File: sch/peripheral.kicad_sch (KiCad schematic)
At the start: 7 parts, among them U1 74LVC1G139

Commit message: some docs
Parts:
- added C? (x2): 100nF, Capacitor_SMD:C_0805_2012Metric, symbol Device:C_Small
- added C?: 30pF, Capacitor_SMD:C_0805_2012Metric, symbol Device:C_Small
- added R?: 1M, Resistor_THT:R_Axial_DIN0204_L3.6mm_D1.6mm_P7.62mm_Horizontal, symbol Device:R
- added SERC?: W65C51NxQ, Package_QFP:LQFP-32_7x7mm_P0.8mm, symbol 65xx:W65C51NxQ
- added SERIAL?: Conn_02x05_Odd_Even, Connector_PinHeader_2.54mm:PinHeader_2x05_P2.54mm_Vertical, symbol Connector_Generic:Conn_02x05_Odd_Even
- added Y?: 1.8432MHz, Crystal:Crystal_HC49-4H_Vertical, symbol Device:Crystal
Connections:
- net +5V: now also C?.2, C?.2, SERC?.12 (VCC), SERC?.13 (VCC), SERIAL?.2 (Pin_2)
- net A0: now also SERC?.10 (RS0)
- net A1: now also SERC?.11 (RS1)
- net A15: now also SERC?.30 (CS1)
- net BUS_R~{W}: now also SERC?.27 (R/~{W})
- net D0: now also SERC?.16 (D0)
- net D1: now also SERC?.17 (D1)
- net D2: now also SERC?.18 (D2)
- net D3: now also SERC?.19 (D3)
- net D4: now also SERC?.20 (D4)
- net D5: now also SERC?.21 (D5)
- net D6: now also SERC?.22 (D6)
- net D7: now also SERC?.23 (D7)
- net GND: now also C?.1, C?.1, C?.2, SERC?.28 (VSS), SERC?.29 (VSS), SERIAL?.10 (Pin_10)
- net ~{RESET}: now also SERC?.32 (~{RES})
- net CLK renamed CLOCK
- net CLOCK: now also SERC?.26 (ϕ2)
- new net: R?.1, SERC?.2 (XTAL1), Y?.2
- new net: C?.1, R?.2, SERC?.3 (XTAL2), Y?.1
- new net: SERC?.1 (RxC), SERIAL?.8 (Pin_8)
- new net: SERC?.14 (~{DCD}), SERIAL?.9 (Pin_9)
- new net: SERC?.15 (~{DSR}), SERIAL?.7 (Pin_7)
- new net: SERC?.4 (~{RTS}), SERIAL?.1 (Pin_1)
- new net: SERC?.5 (~{CTS}), SERIAL?.3 (Pin_3)
- new net: SERC?.6 (TxD), SERIAL?.6 (Pin_6)
- new net: SERC?.7 (~{DTR}), SERIAL?.5 (Pin_5)
- new net: SERC?.9 (RxD), SERIAL?.4 (Pin_4)
- new net ~{SERIAL_CS}: SERC?.31 (~{CS2})
- new net ~{SRL_IRQ}: SERC?.25 (~{IRQ})
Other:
- note added: "PRP: 0x8000 - 0x8FFF SER: 0x9000 - 0x9FFF"
- note added: "Peripheral and Serial Controller"
- note added: "Serial Controller"
- moved on the sheet: C21, C22, PERIPHERAL1, PRP1, U1, USB1, USB_P1

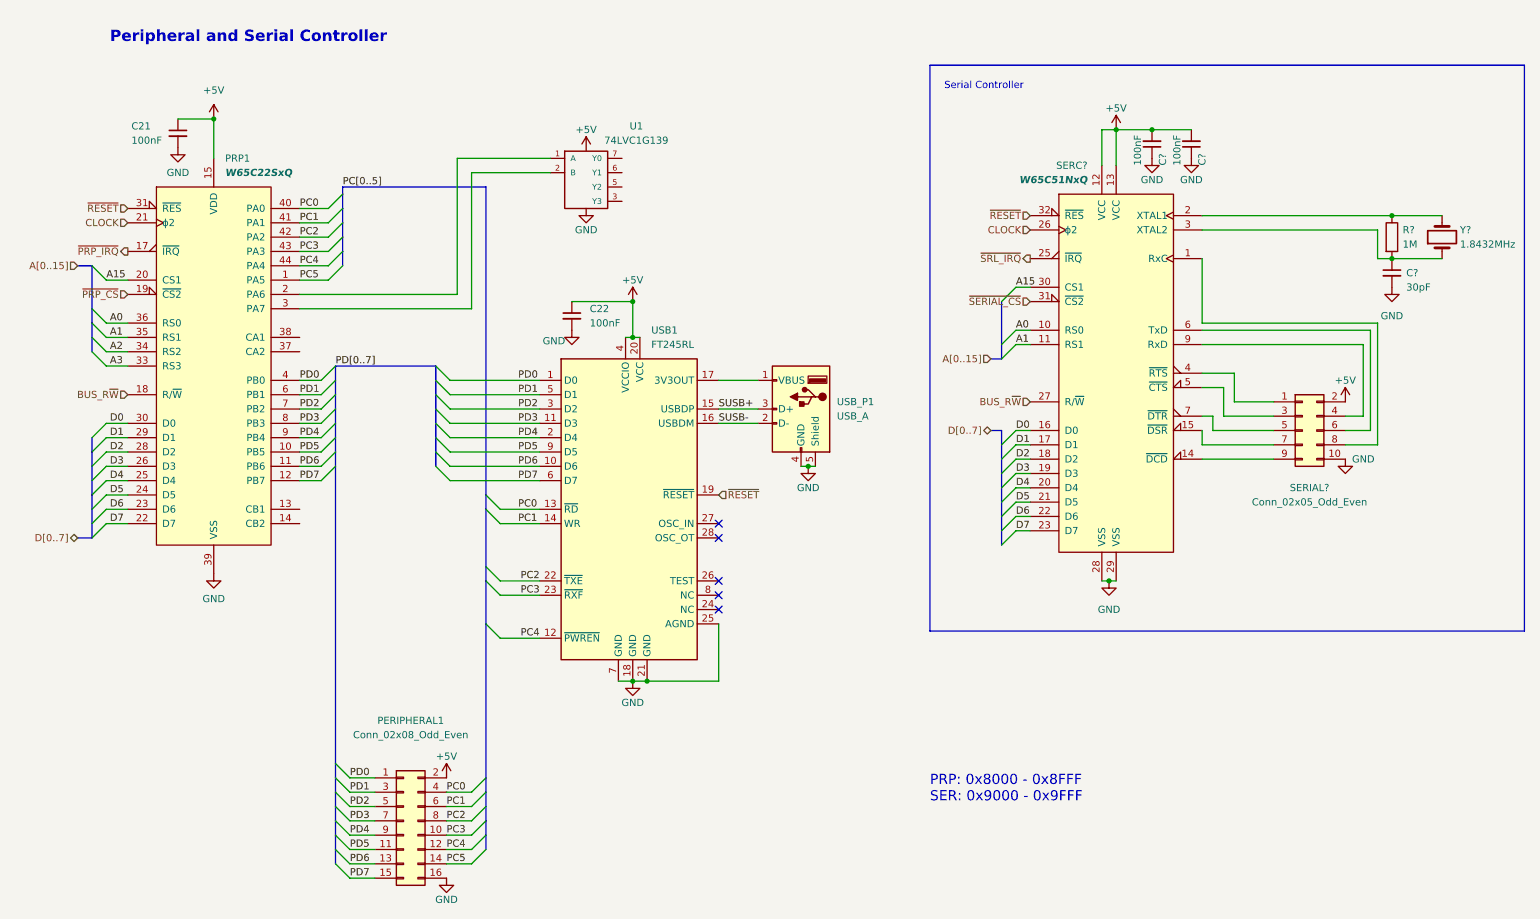
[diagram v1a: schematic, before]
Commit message: update schematic
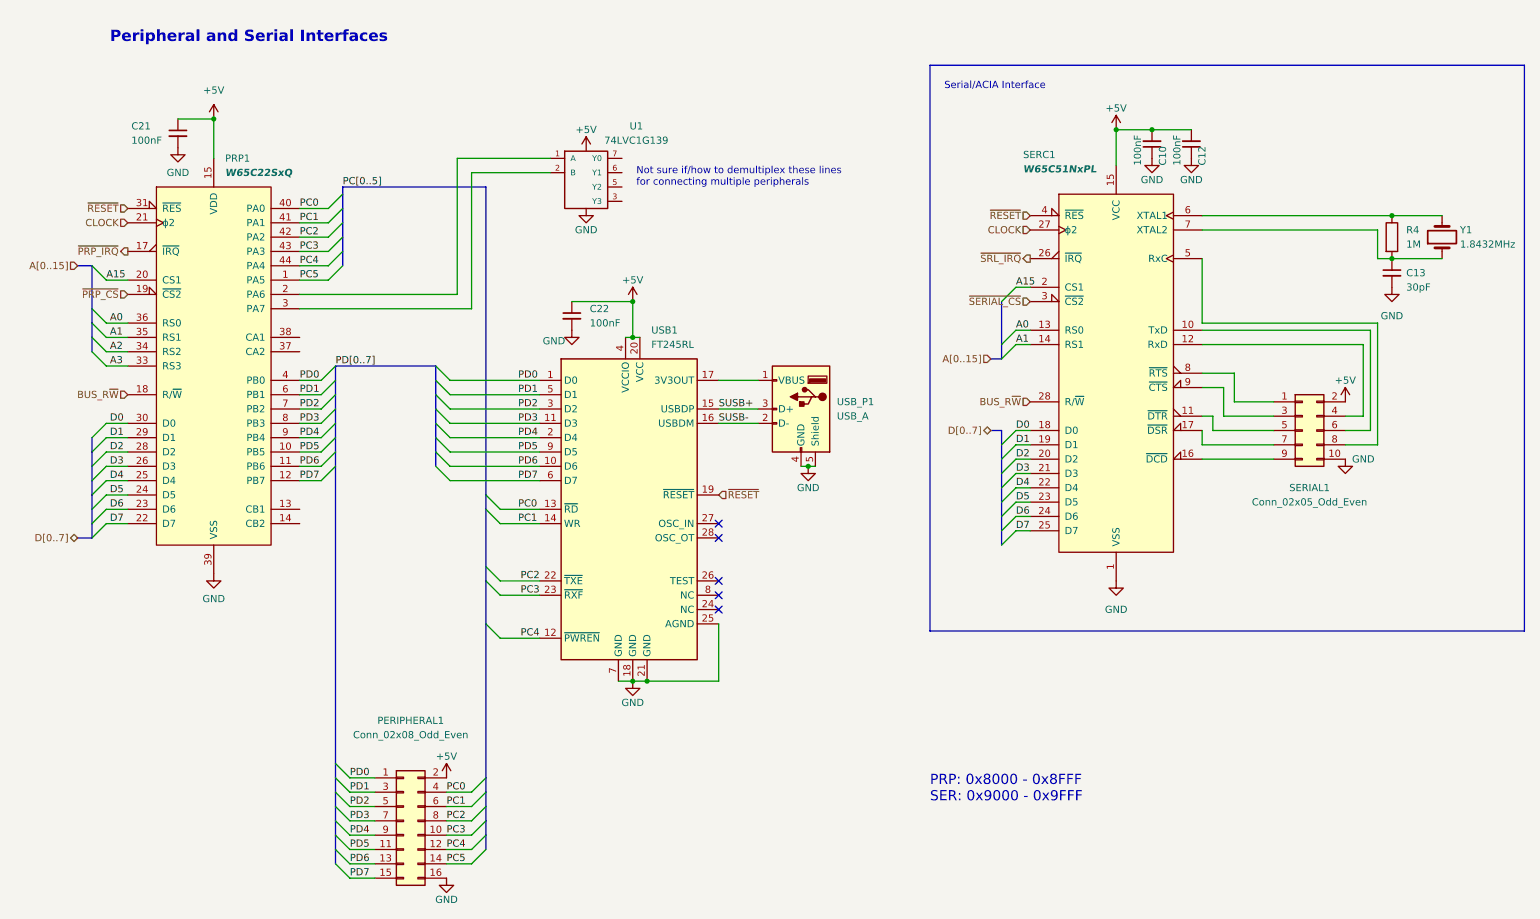
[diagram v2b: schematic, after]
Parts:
- removed SERC?: W65C51NxQ, Package_QFP:LQFP-32_7x7mm_P0.8mm, symbol 65xx:W65C51NxQ
- added SERC1: W65C51NxPL, Package_LCC:PLCC-28, symbol 65xx:W65C51NxPL
- gave numbers to parts that had none: 6
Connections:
- net +5V: now also SERC1.15 (VCC)
- net A0: now also SERC1.13 (RS0)
- net A1: now also SERC1.14 (RS1)
- net A15: now also SERC1.2 (CS1)
- net BUS_R~{W}: now also SERC1.28 (R/~{W})
- net CLOCK: now also SERC1.27 (ϕ2)
- net D0: now also SERC1.18 (D0)
- net D1: now also SERC1.19 (D1)
- net D2: now also SERC1.20 (D2)
- net D3: now also SERC1.21 (D3)
- net D4: now also SERC1.22 (D4)
- net D5: now also SERC1.23 (D5)
- net D6: now also SERC1.24 (D6)
- net D7: now also SERC1.25 (D7)
- net GND: now also SERC1.1 (VSS)
- net ~{RESET}: now also SERC1.4 (~{RES})
- net ~{SERIAL_CS}: now also SERC1.3 (~{CS2})
- net ~{SRL_IRQ}: now also SERC1.26 (~{IRQ})
- net at R4.1, Y1.2: now also SERC1.6 (XTAL1)
- net at C13.1, R4.2, Y1.1: now also SERC1.7 (XTAL2)
- net at SERIAL1.8 (Pin_8): now also SERC1.5 (RxC)
- net at SERIAL1.9 (Pin_9): now also SERC1.16 (~{DCD})
- net at SERIAL1.7 (Pin_7): now also SERC1.17 (~{DSR})
- net at SERIAL1.1 (Pin_1): now also SERC1.8 (~{RTS})
- net at SERIAL1.3 (Pin_3): now also SERC1.9 (~{CTS})
- net at SERIAL1.6 (Pin_6): now also SERC1.10 (TxD)
- net at SERIAL1.5 (Pin_5): now also SERC1.11 (~{DTR})
- net at SERIAL1.4 (Pin_4): now also SERC1.12 (RxD)
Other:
- note added: "Not sure if/how to demultiplex these lines for connecting multiple peripherals"
- note added: "Peripheral and Serial Interfaces"
- note added: "Serial/ACIA Interface"
- note removed: "Peripheral and Serial Controller"
- note removed: "Serial Controller"

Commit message: serial rollback
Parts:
- removed C10, C12: 100nF, Capacitor_SMD:C_0805_2012Metric, symbol Device:C_Small
- removed C13: 30pF, Capacitor_SMD:C_0805_2012Metric, symbol Device:C_Small
- removed R4: 1M, Resistor_THT:R_Axial_DIN0204_L3.6mm_D1.6mm_P7.62mm_Horizontal, symbol Device:R
- removed SERC1: W65C51NxPL, Package_LCC:PLCC-28, symbol 65xx:W65C51NxPL
- removed SERIAL1: Conn_02x05_Odd_Even, Connector_PinHeader_2.54mm:PinHeader_2x05_P2.54mm_Vertical, symbol Connector_Generic:Conn_02x05_Odd_Even
- removed U1: 74LVC1G139, symbol 74xGxx:74LVC1G139
- removed Y1: 1.8432MHz, Crystal:Crystal_HC49-4H_Vertical, symbol Device:Crystal
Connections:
- net A15 renamed A13
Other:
- note added: "0x6000 - 0x600F"
- note added: "Peripheral Interface"
- note removed: "Not sure if/how to demultiplex these lines for connecting multiple peripherals"
- note removed: "PRP: 0x8000 - 0x8FFF SER: 0x9000 - 0x9FFF"
- note removed: "Peripheral and Serial Interfaces"
- note removed: "Serial/ACIA Interface"
- moved on the sheet: C21, C22, PERIPHERAL1, PRP1, USB1, USB_P1

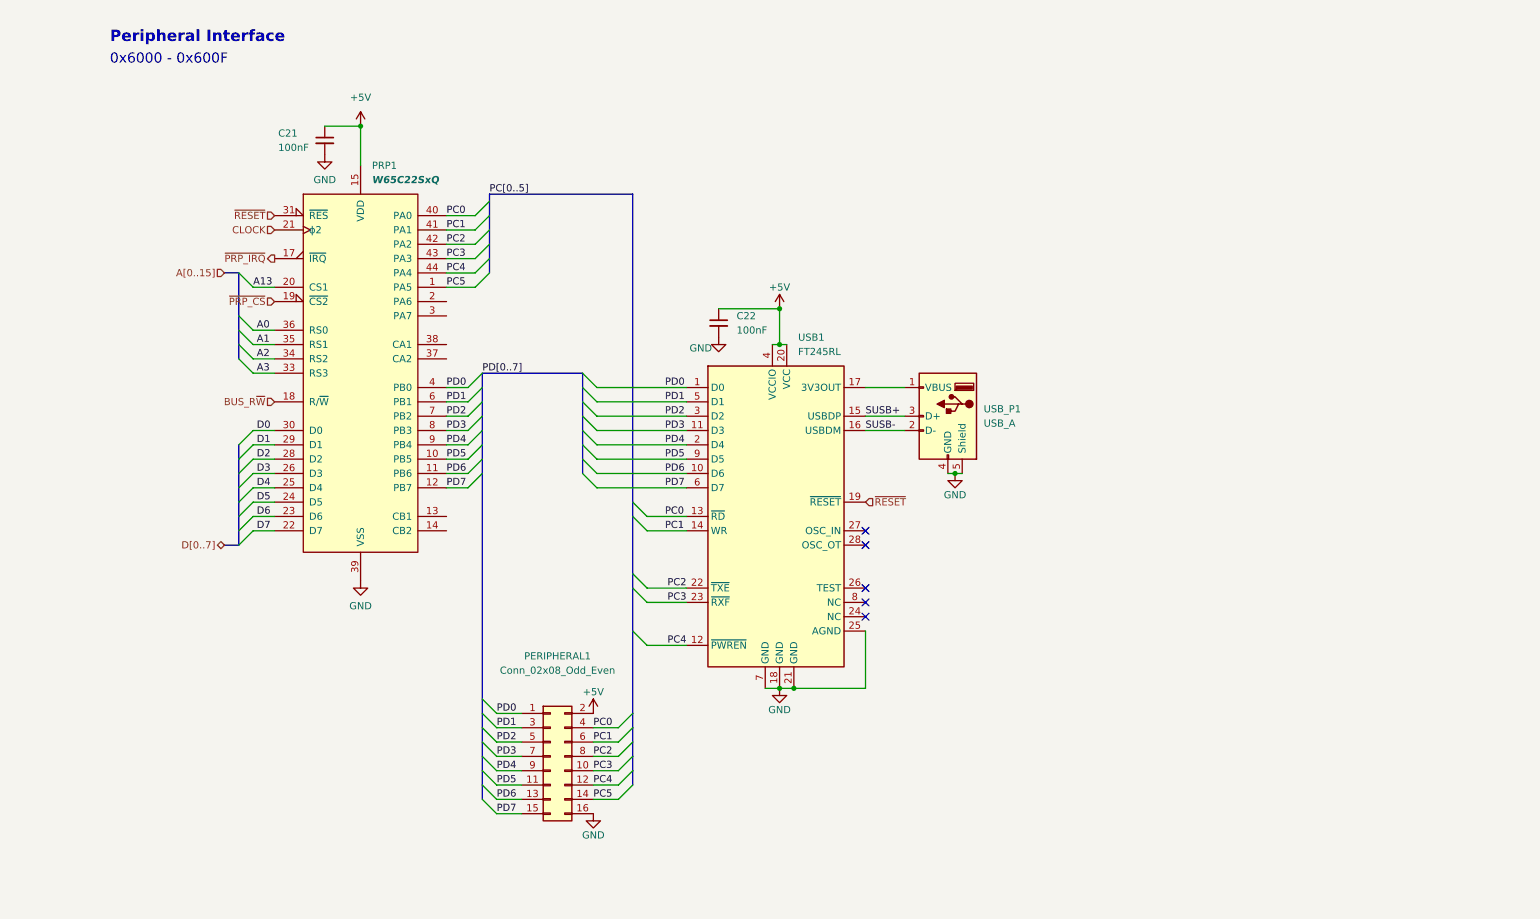
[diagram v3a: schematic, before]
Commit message: fix peripherals, add SPI
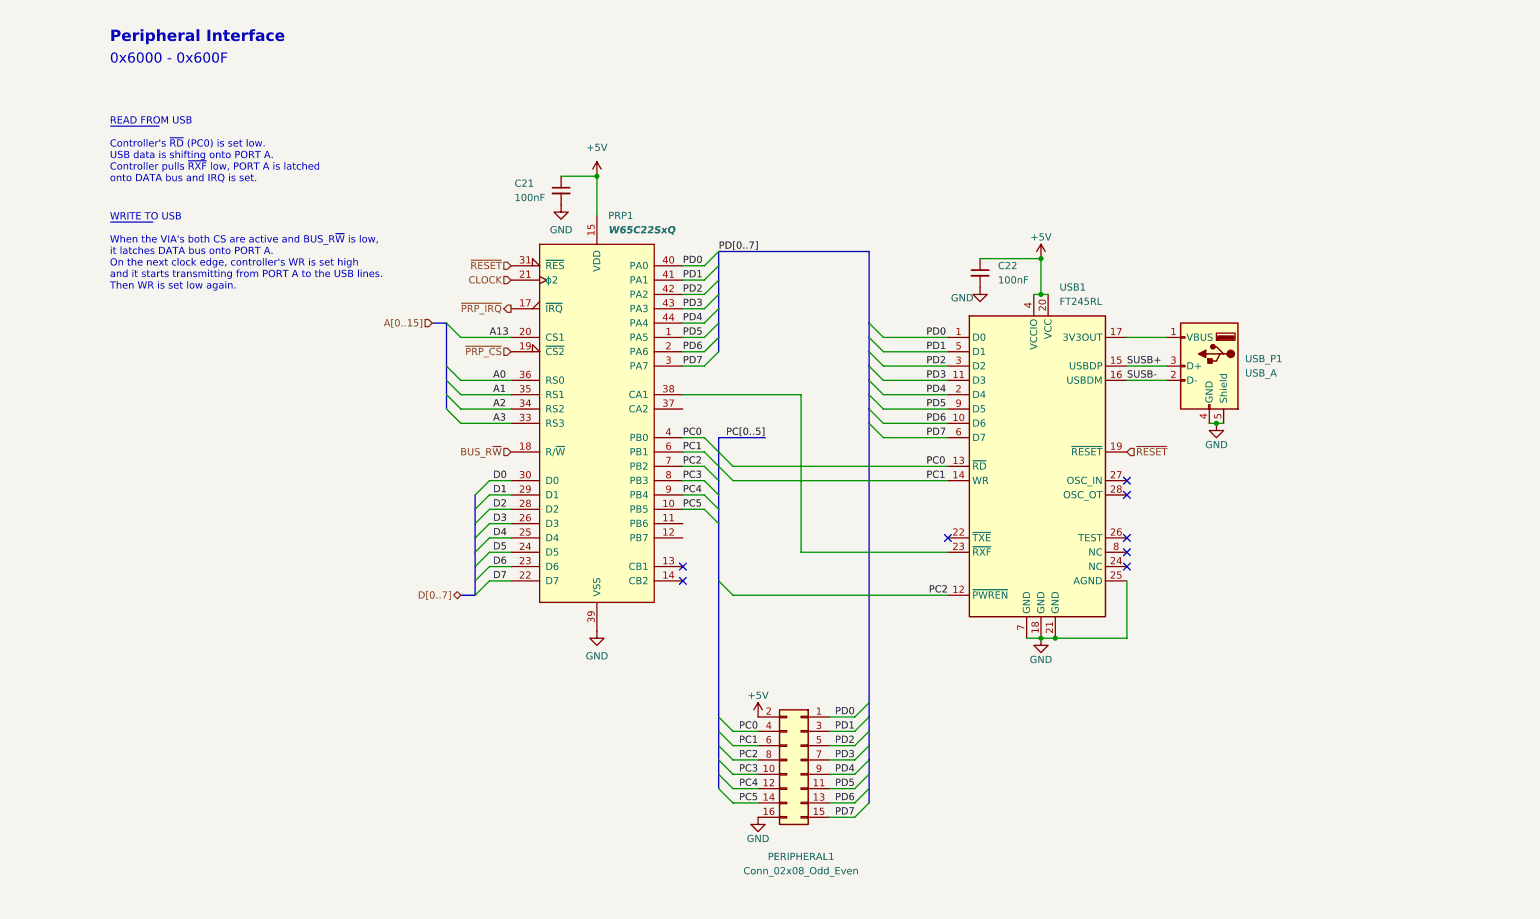
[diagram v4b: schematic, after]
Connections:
- net PC0: now also PRP1.4 (PB0); no longer PRP1.40 (PA0)
- net PC1: now also PRP1.6 (PB1); no longer PRP1.41 (PA1)
- net PC2: now also PRP1.7 (PB2), USB1.12 (~{PWREN}); no longer PRP1.42 (PA2), USB1.22 (~{TXE})
- net PC3: now also PRP1.8 (PB3); no longer PRP1.43 (PA3), USB1.23 (~{RXF})
- net PC4: now also PRP1.9 (PB4); no longer PRP1.44 (PA4), USB1.12 (~{PWREN})
- net PC5: now also PRP1.10 (PB5); no longer PRP1.1 (PA5)
- net PD0: now also PRP1.40 (PA0); no longer PRP1.4 (PB0)
- net PD1: now also PRP1.41 (PA1); no longer PRP1.6 (PB1)
- net PD2: now also PRP1.42 (PA2); no longer PRP1.7 (PB2)
- net PD3: now also PRP1.43 (PA3); no longer PRP1.8 (PB3)
- net PD4: now also PRP1.44 (PA4); no longer PRP1.9 (PB4)
- net PD5: now also PRP1.1 (PA5); no longer PRP1.10 (PB5)
- net PD6: now also PRP1.2 (PA6); no longer PRP1.11 (PB6)
- net PD7: now also PRP1.3 (PA7); no longer PRP1.12 (PB7)
- net at PRP1.38 (CA1): now also USB1.23 (~{RXF})
- no-connect marks 5 -> 8
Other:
- note added: "READ FROM USB ~{ } Controller's ~{RD} (PC0) is set low. USB data is shifting onto PORT A. Controller pulls ~{RXF} low, PORT A is latched onto DATA bus and IRQ is set."
- note added: "WRITE TO USB ~{ } When the VIA's both CS are active and BUS_R~{W} is low, it latches DATA bus onto PORT A. On the next clock edge, controller's WR is set high and it starts transmitting from PORT A to the USB lines. Then WR is set low again."
- moved on the sheet: C21, C22, PERIPHERAL1, PRP1, USB1, USB_P1

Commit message: Cleanup board
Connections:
- no-connect marks 8 -> 11
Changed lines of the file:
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@@
   (no_connect (at 180.34 113.03))
   (no_connect (at 212.09 113.03))
+  (no_connect (at 133.35 110.49))
+  (no_connect (at 133.35 113.03))
+  (no_connect (at 133.35 90.17))
   (no_connect (at 212.09 102.87))
   (no_connect (at 212.09 105.41))

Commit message: bigger header pins
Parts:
- PERP1: renamed from PERIPHERAL1; value Conn_02x08_Odd_Even -> (none); footprint Connector_PinHeader_2.00mm:PinHeader_2x08_P2.00mm_Vertical -> (none)
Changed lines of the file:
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@@
   (symbol (lib_id "Connector_Generic:Conn_02x08_Odd_Even") (at 154.305 152.4 0) (mirror y) (unit 1)
     (in_bom yes) (on_board yes)
-    (property "Reference" "PERIPHERAL1" (id 0) (at 154.305 169.545 0))
-    (property "Value" "Conn_02x08_Odd_Even" (id 1) (at 154.305 172.085 0))
-    (property "Footprint" "Connector_PinHeader_2.00mm:PinHeader_2x08_P2.00mm_Vertical" (id 2) (at 154.305 152.4 0)
+    (property "Reference" "PERP1" (id 0) (at 154.305 169.545 0))
+    (property "Value" "" (id 1) (at 154.305 172.085 0))
+    (property "Footprint" "" (id 2) (at 154.305 152.4 0)
       (effects (font (size 1.27 1.27)) hide)
     )

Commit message: small updates
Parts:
- PERP1: value (none) -> Conn_02x08_Odd_Even; footprint (none) -> Connector_PinHeader_2.54mm:PinHeader_2x08_P2.54mm_Vertical
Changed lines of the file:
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@@
+    (stroke (width 0) (type default) (color 0 0 0 0))
+  )
+  (bus (pts (xy 166.37 141.605) (xy 166.37 142.24))
     (stroke (width 0) (type default) (color 0 0 0 0))
   )
@@
     (stroke (width 0) (type default) (color 0 0 0 0))
   )
-  (bus (pts (xy 166.37 92.71) (xy 166.37 142.24))
-    (stroke (width 0) (type default) (color 0 0 0 0))
-  )
   (bus (pts (xy 139.7 110.49) (xy 139.7 120.65))
     (stroke (width 0) (type default) (color 0 0 0 0))
@@
     (stroke (width 0) (type default) (color 0 0 0 0))
   )
+  (bus (pts (xy 174.625 141.605) (xy 166.37 141.605))
+    (stroke (width 0) (type default) (color 0 0 0 0))
+  )
   (bus (pts (xy 139.7 149.86) (xy 139.7 152.4))
     (stroke (width 0) (type default) (color 0 0 0 0))
@@
   (bus (pts (xy 139.7 120.65) (xy 139.7 144.78))
     (stroke (width 0) (type default) (color 0 0 0 0))
-  )
-  (text "Peripheral Interface" (at 31.75 25.4 0)
-    (effects (font (size 2 2) (thickness 0.4) bold) (justify left bottom))
   )
   (text "0x6000 - 0x600F" (at 31.75 29.21 0)
     (effects (font (size 1.8 1.8)) (justify left bottom))
   )
+  (text "Peripheral Interface" (at 31.75 26.035 0)
+    (effects (font (size 2 2) (thickness 0.254) bold) (justify left bottom))
+  )
   (text "WRITE TO USB\n~{              }\nWhen the VIA's both CS are active and BUS_R~{W} is low, \nit latches DATA bus onto PORT A.\nOn the next clock edge, controller's WR is set high \nand it starts transmitting from PORT A to the USB lines.\nThen WR is set low again."
     (at 31.75 69.215 0)
@@
   (label "D6" (at 99.695 118.11 0)
     (effects (font (size 1.27 1.27)) (justify left bottom))
+  )
+  (label "PD[0..7]" (at 174.625 141.605 180)
+    (effects (font (size 1.27 1.27)) (justify right bottom))
   )
   (label "PC5" (at 133.35 107.95 0)
@@
     (in_bom yes) (on_board yes)
     (property "Reference" "PERP1" (id 0) (at 154.305 169.545 0))
-    (property "Value" "" (id 1) (at 154.305 172.085 0))
-    (property "Footprint" "" (id 2) (at 154.305 152.4 0)
-      (effects (font (size 1.27 1.27)) hide)
-    )
+    (property "Value" "Conn_02x08_Odd_Even" (id 1) (at 154.305 172.085 0))
+    (property "Footprint" "Connector_PinHeader_2.54mm:PinHeader_2x08_P2.54mm_Vertical" (id 2) (at 154.305 152.4 0)
+      (effects (font (size 1.27 1.27)) hide)
+    )
